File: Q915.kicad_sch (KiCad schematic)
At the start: 5 parts, among them J1 W5500, J2 Jack-DC, U1 AE-HX711-SIP, U2 AE-HX711-SIP

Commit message: 2nd
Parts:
- added J3: I2C, symbol Connector_Generic:Conn_01x04
- added R1: 10k, symbol Device:R_US
- added SW1: RESET, symbol Switch:SW_Push
- J2: value Jack-DC -> DC5V
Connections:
- net GND: now also J3.1 (Pin_1), SW1.2
- net at A1.13 (SDA/A4): now also J3.3 (Pin_3)
- net at A1.14 (SCL/A5): now also J3.4 (Pin_4)
- net SS: now reaches A1.25 (D10), J1.7 (Pin_7)
- net MOSI: now reaches A1.26 (D11), J1.5 (Pin_5)
- net MISO: now reaches A1.27 (D12), J1.3 (Pin_3)
- net CLK: now reaches A1.28 (D13), J1.9 (Pin_9)
- net !RESET: now reaches A1.3 (~{RESET}), J1.6 (Pin_6)
- net !RESET: now also J3.2 (Pin_2), R1.2, SW1.1
- net at A1.5 (+5V), J1.2 (Pin_2), J2.1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: now also R1.1
- no-connect marks 32 -> 30
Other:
- moved on the sheet: A1

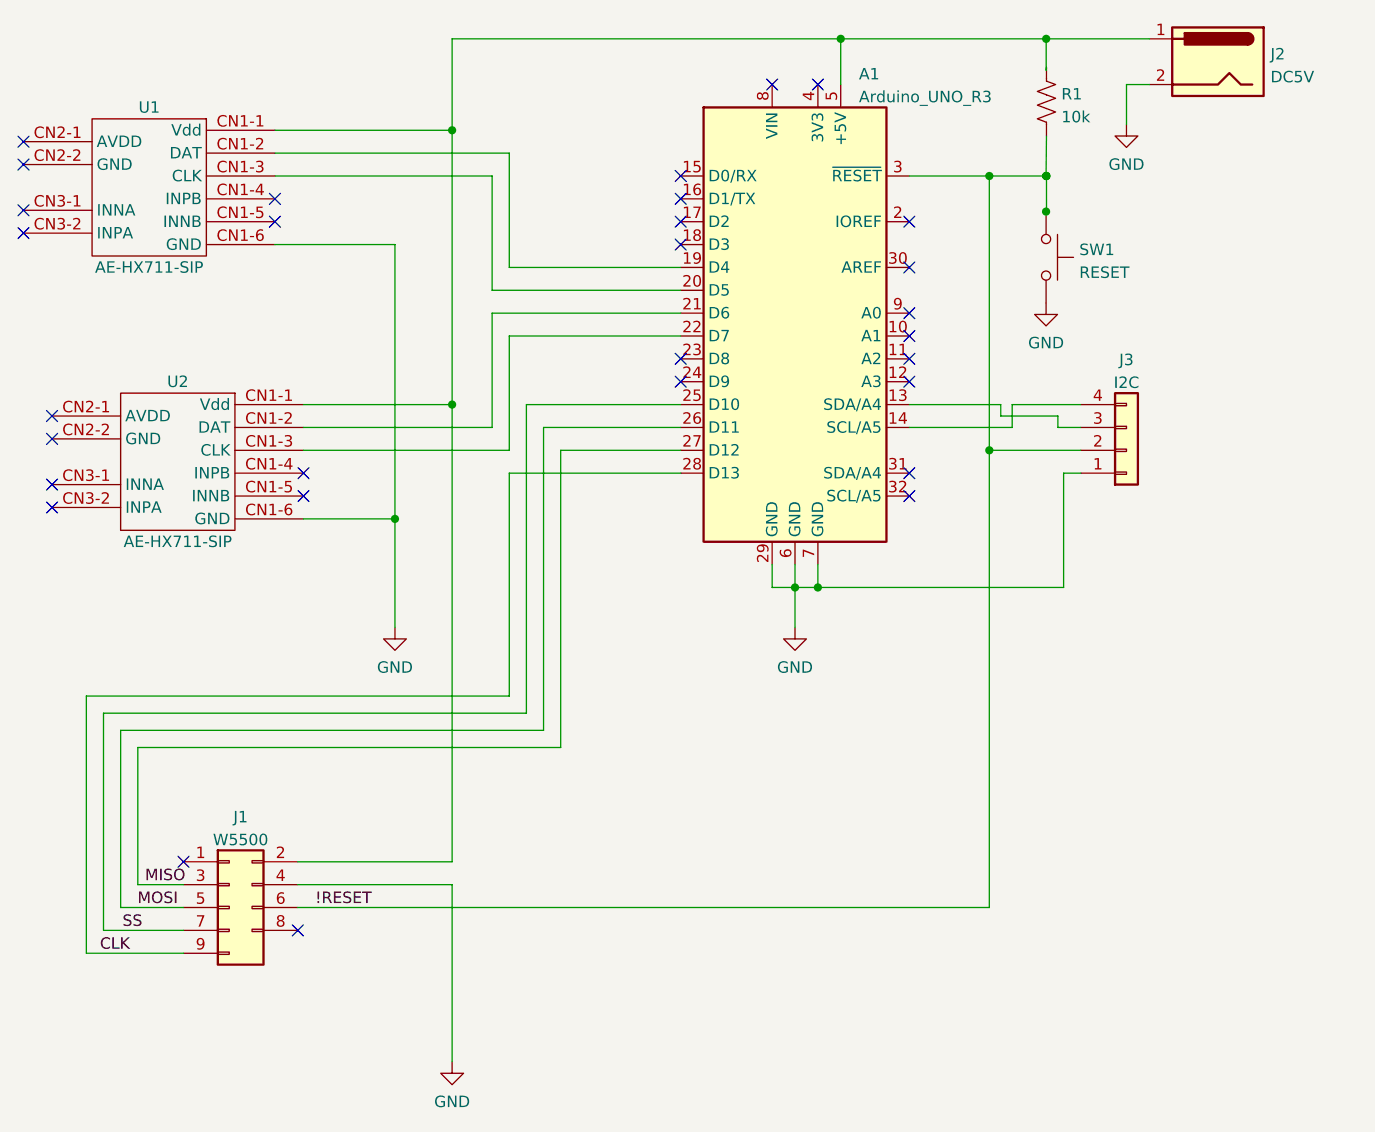
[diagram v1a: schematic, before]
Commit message: ICSP追加とREADME変更
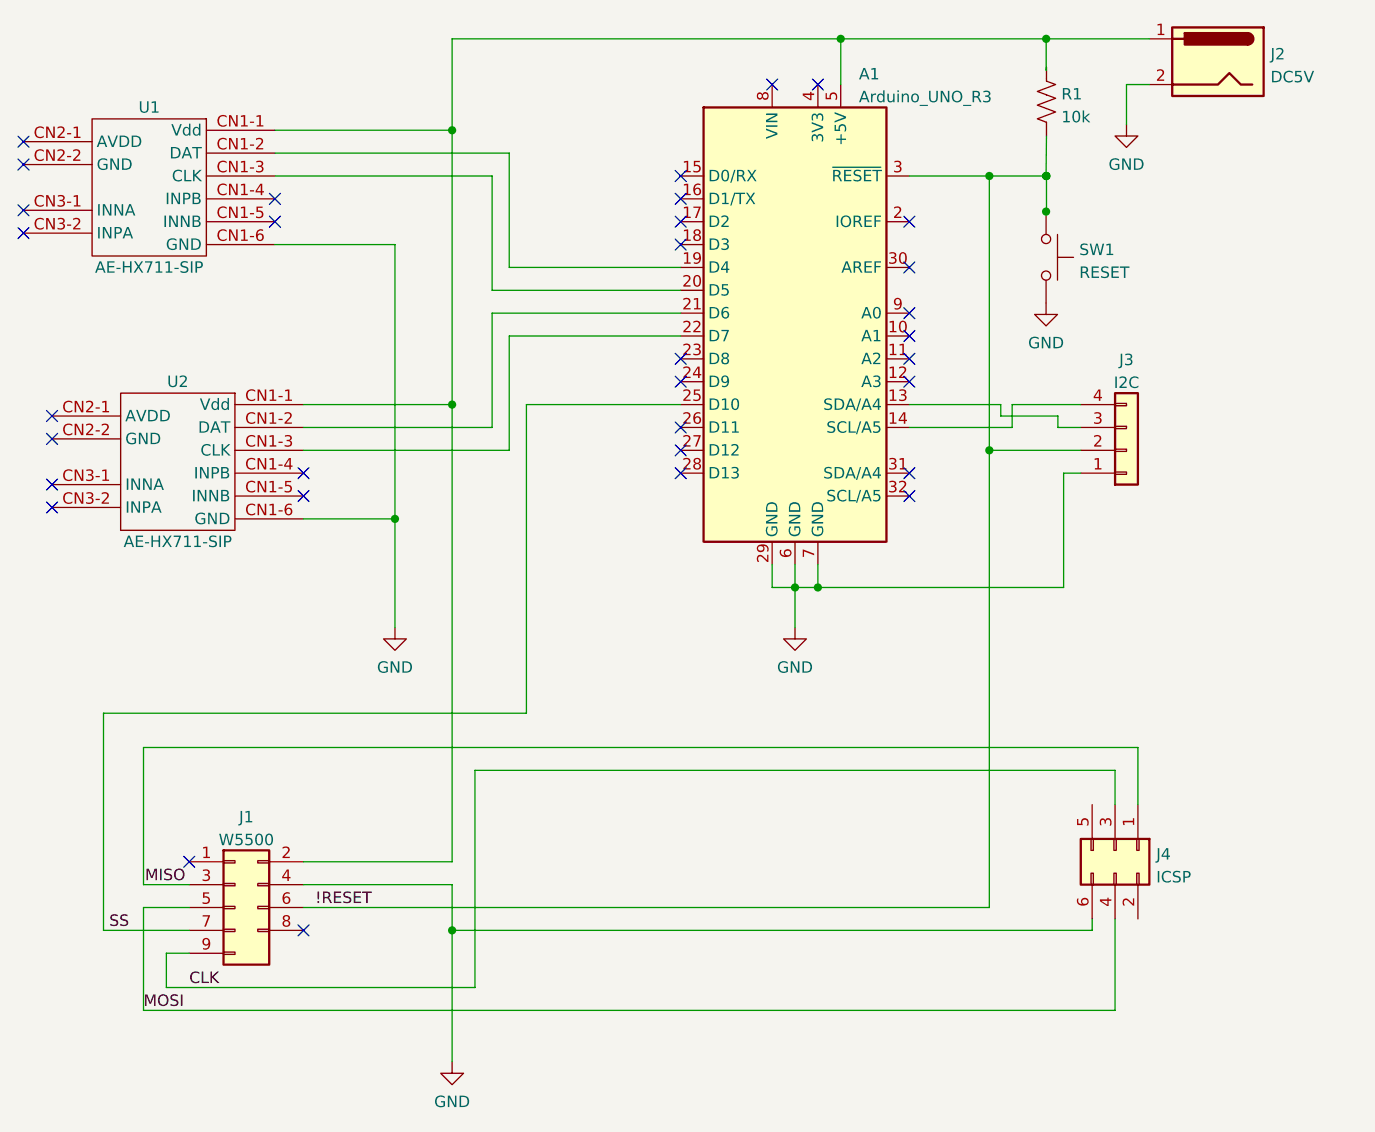
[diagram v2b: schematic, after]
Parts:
- added J4: ICSP, symbol Connector_Generic:Conn_02x03_Odd_Even
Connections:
- net CLK: now also J4.3 (Pin_3); no longer A1.28 (D13)
- net GND: now also J4.6 (Pin_6)
- net MISO: now also J4.1 (Pin_1); no longer A1.27 (D12)
- net MOSI: now also J4.4 (Pin_4); no longer A1.26 (D11)
- no-connect marks 30 -> 33
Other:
- moved on the sheet: J1
